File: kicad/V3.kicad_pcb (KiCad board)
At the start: 2 copper layers, 172.9 x 118.3 mm, 51 parts, among them SW1 Slide_Switch_SPDT_P3mm_10x5x1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

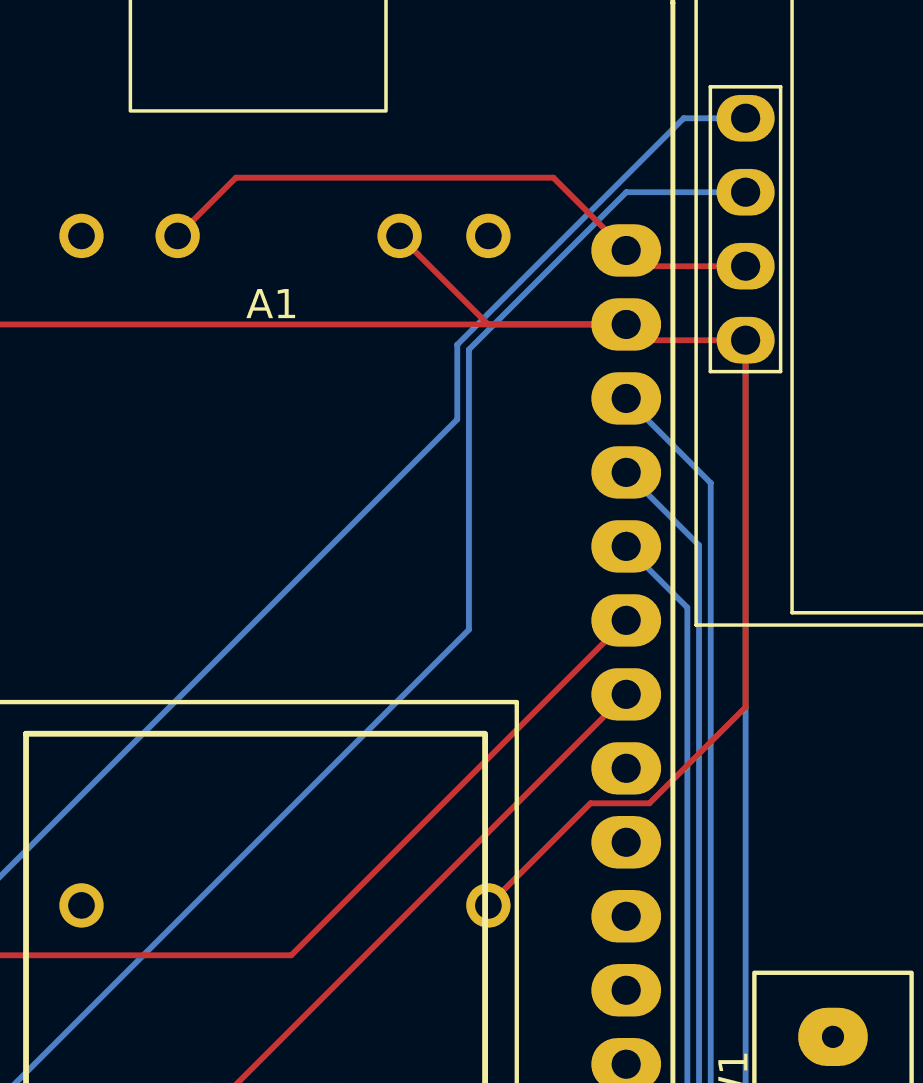
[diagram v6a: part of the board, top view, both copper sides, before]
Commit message: removed false connections
that footprint is wrong
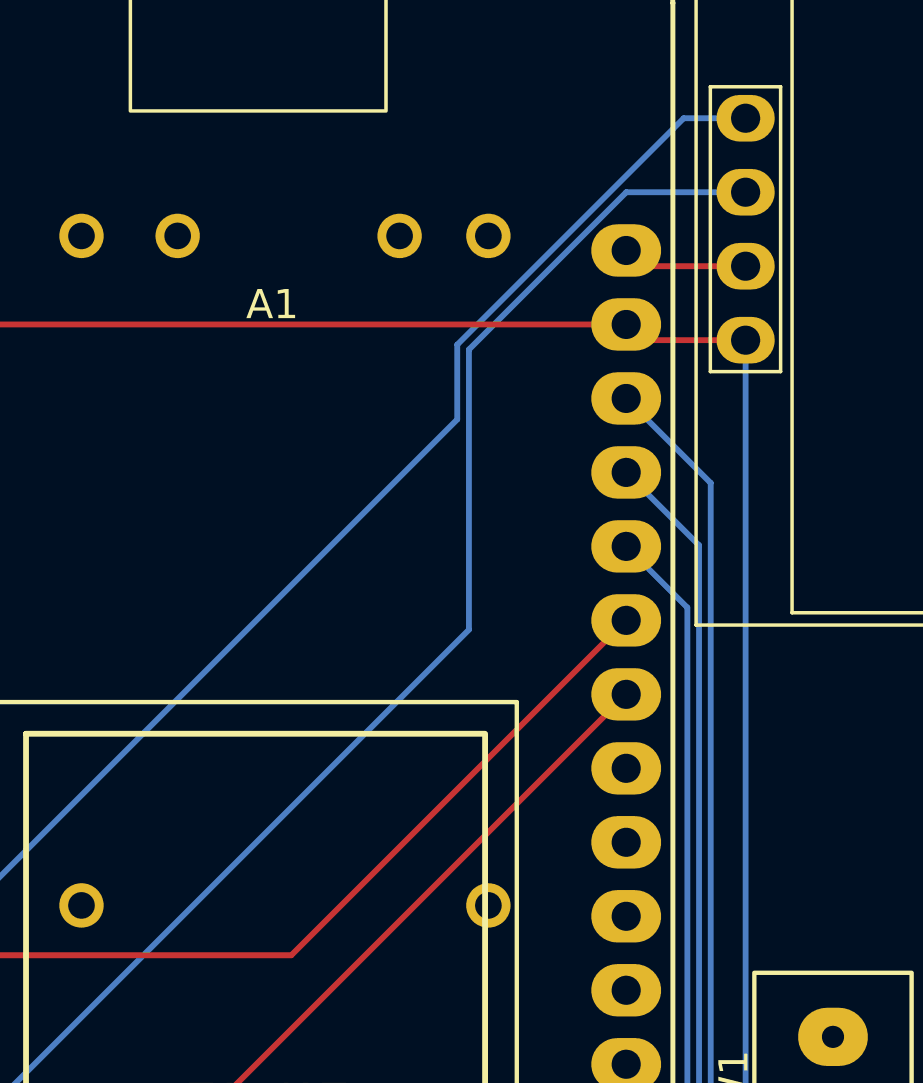
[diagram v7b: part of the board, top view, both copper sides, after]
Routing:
- net Earth: track 142.2 -> 108.9 mm
- net VCC: track 21.6 -> 4.32 mm
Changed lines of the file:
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@@
-	)
-	(segment
-		(start 209.5 62)
-		(end 220.4 62)
-		(width 0.2)
-		(layer "F.Cu")
-		(net 8)
-	)
-	(segment
-		(start 220.4 62)
-		(end 222.9 64.5)
-		(width 0.2)
-		(layer "F.Cu")
-		(net 8)
 	)
 	(segment
@@
 	)
 	(segment
-		(start 207.5 64)
-		(end 209.5 62)
-		(width 0.2)
-		(layer "F.Cu")
-		(net 8)
-	)
-	(segment
 		(start 211.401 88.699)
 		(end 222.9 77.2)
@@
 	)
 	(segment
-		(start 227 80.17847)
-		(end 227 67.58)
-		(width 0.2)
-		(layer "F.Cu")
-		(net 11)
-	)
-	(segment
-		(start 221.674 83.481)
-		(end 223.69747 83.481)
-		(width 0.2)
-		(layer "F.Cu")
-		(net 11)
-	)
-	(segment
-		(start 218.16 67.04)
-		(end 215.12 64)
-		(width 0.2)
-		(layer "F.Cu")
-		(net 11)
-	)
-	(segment
-		(start 218.168 86.987)
-		(end 221.674 83.481)
-		(width 0.2)
-		(layer "F.Cu")
-		(net 11)
-	)
-	(segment
 		(start 227 67.58)
 		(end 223.44 67.58)
 		(width 0.2)
 		(layer "F.Cu")
-		(net 11)
-	)
-	(segment
-		(start 223.69747 83.481)
-		(end 227 80.17847)
-		(width 0.2)
-		(layer "F.Cu")
-		(net 11)
-	)
-	(segment
-		(start 222.9 67.04)
-		(end 218.16 67.04)
-		(width 0.2)
-		(layer "F.Cu")

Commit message: fixed connections and pin#
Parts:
- U1: moved to F.Cu
- moved SW1 5.52 mm to (229.5, 92.0)
- moved U1 0.44 mm to (210.6, 76.1)
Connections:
- U1 pad 1: Net-(U1-Out+) -> Earth
- U1 pad 2: Earth -> VCC
- U1 pad 3: Net-(BT1-+) -> Earth
- U1 pad 4: VCC -> Net-(BT1--)
- U1 pad 5: Earth -> Net-(BT1-+)
- U1 pad 6: Net-(BT1--) -> Net-(U1-Out+)
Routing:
- net -3V3: track 50.9 -> 122.3 mm
- net Net-(U1-Out+): track 0.00 -> 61.1 mm
- net VCC: track 4.32 -> 34.9 mm, vias 0 -> 1
- net Earth: track 108.9 -> 133.0 mm, vias 0 -> 1
- net /TX: track 35.2 -> 29.9 mm
- net /RX: track 31.9 -> 30.3 mm
